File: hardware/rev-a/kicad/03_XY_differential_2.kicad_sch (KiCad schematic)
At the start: 6 parts

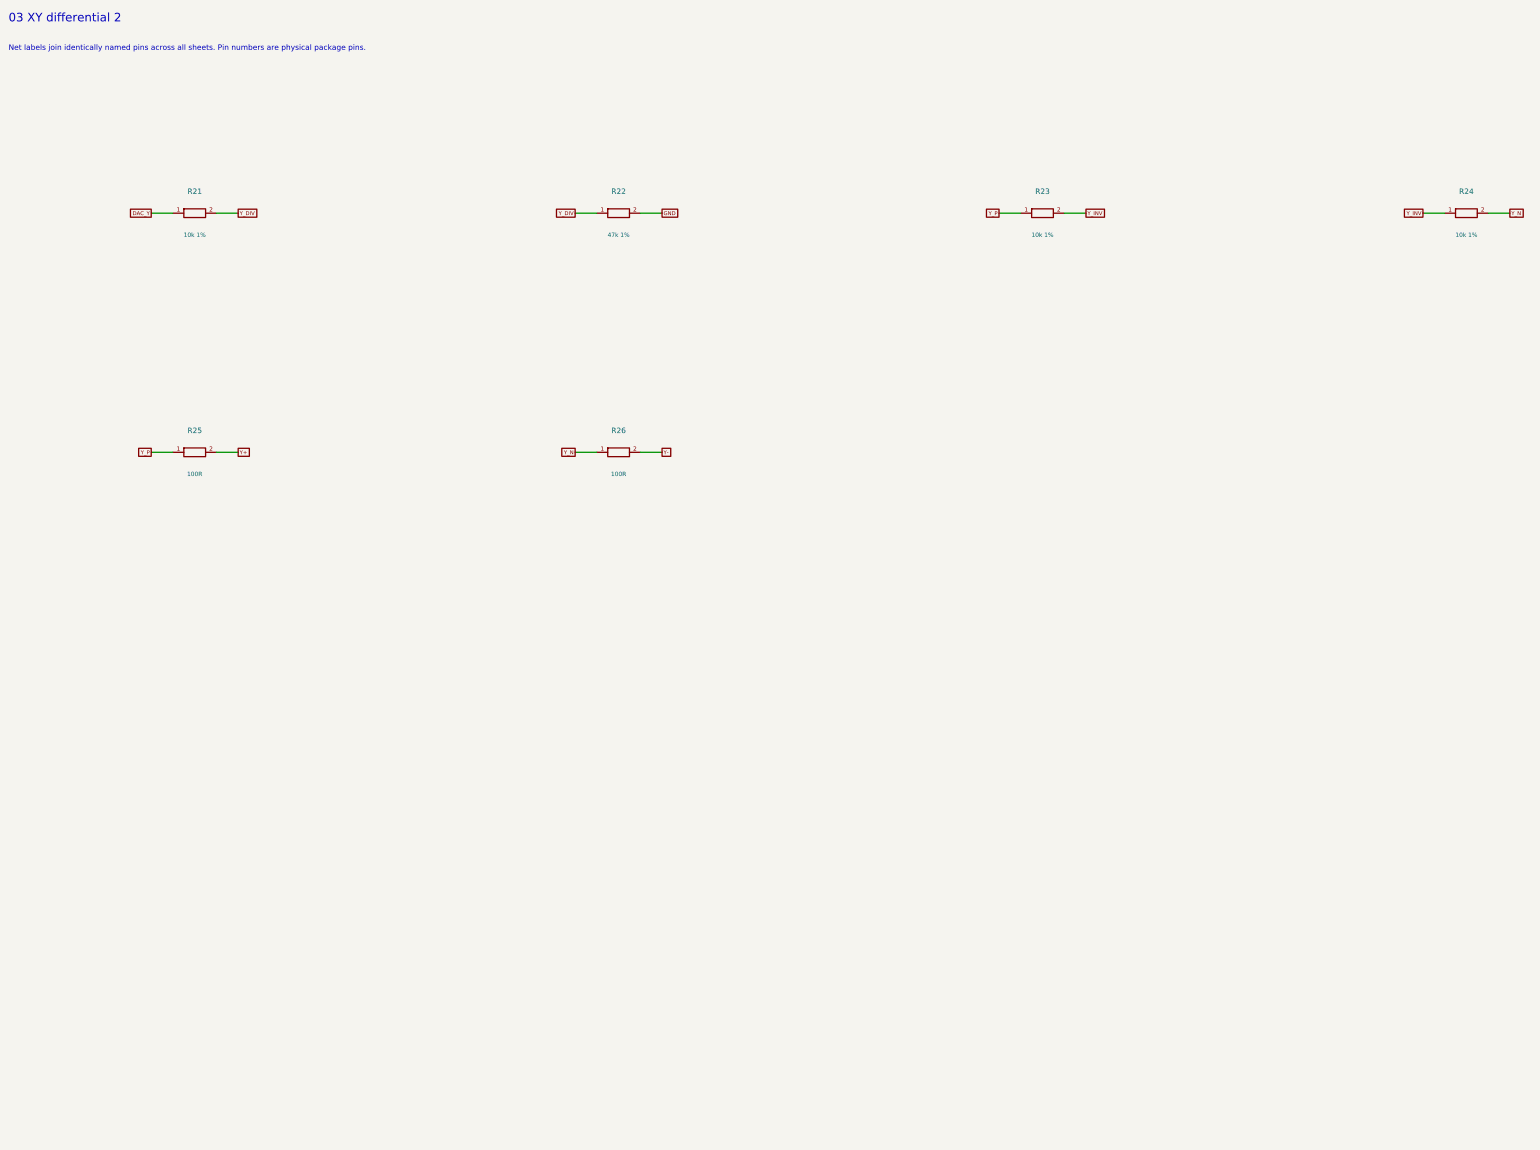
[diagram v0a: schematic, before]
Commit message: Redraw Rev.A schematics with functional blocks and explicit wiring
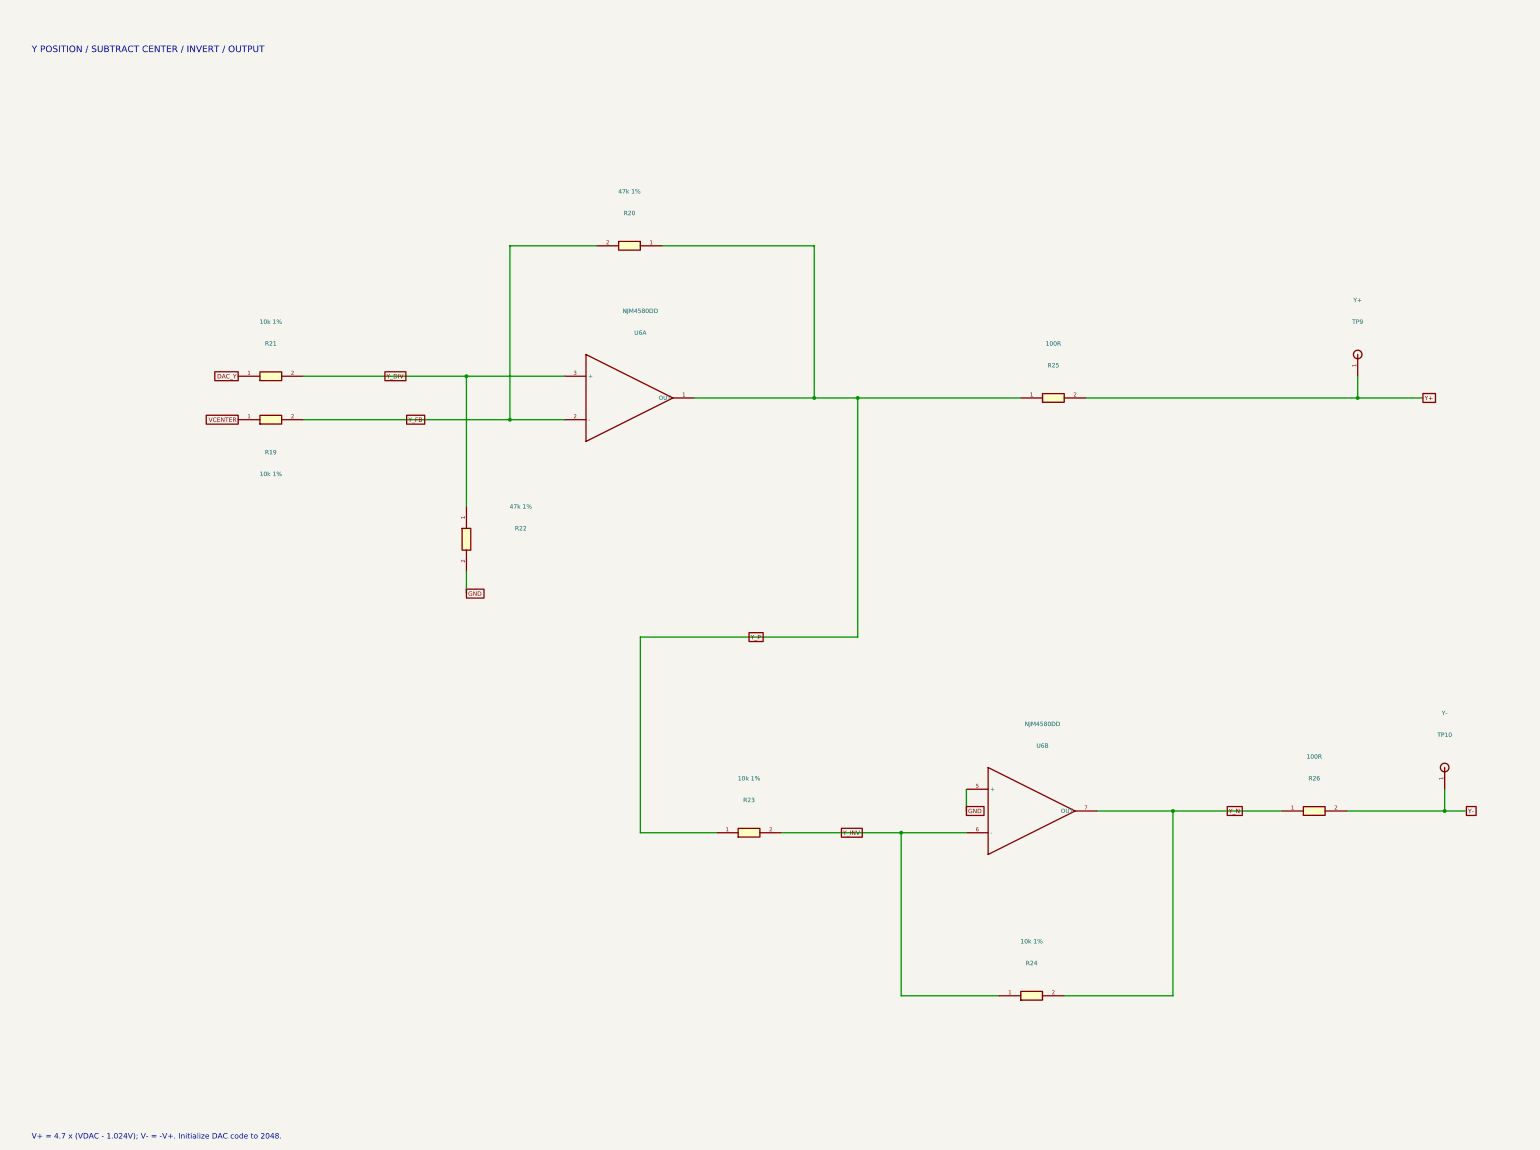
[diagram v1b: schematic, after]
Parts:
- added R19: 10k 1%, RevA:R_Axial_DIN0207_L6.3mm_D2.5mm_P10.16mm_Horizontal, symbol RevA:R
- added R20: 47k 1%, RevA:R_Axial_DIN0207_L6.3mm_D2.5mm_P10.16mm_Horizontal, symbol RevA:R
- added TP10: Y-, RevA:TestPoint_THTPad_D2.0mm_Drill1.0mm, symbol RevA:TP
- added TP9: Y+, RevA:TestPoint_THTPad_D2.0mm_Drill1.0mm, symbol RevA:TP
- added U6: NJM4580DD, RevA:DIP-8_W7.62mm, symbol RevA:AMP
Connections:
- net GND: now also U6.5 (+)
- net Y+: now also TP9.1
- net Y-: now also TP10.1
- net Y_DIV: now also U6.3 (+)
- net Y_INV: now also U6.6 (-)
- net Y_N: now also U6.7 (OUT)
- net Y_P: now also R20.1, U6.1 (OUT)
- new net VCENTER: R19.1
- new net Y_FB: R19.2, R20.2, U6.2 (-)
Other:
- note added: "V+ = 4.7 x (VDAC - 1.024V); V- = -V+. Initialize DAC code to 2048."
- note added: "Y POSITION / SUBTRACT CENTER / INVERT / OUTPUT"
- note removed: "03 XY differential 2"
- note removed: "Net labels join identically named pins across all sheets. Pin numbers are physical package pins."
- company: CoreS3 ILDA evaluation -> (none)
- title: 03_XY_differential_2 -> Y / Differential position driver
